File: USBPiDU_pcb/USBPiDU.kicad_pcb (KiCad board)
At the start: 2 copper layers, 71.5 x 56 mm, 39 parts, among them J1 USB_OTG, J2 ICSP, J3 Load Rail Input, P1 USB_A, P2 USB_A, P3 USB_A, P4 USB_A, P5 USB_A, P6 USB_A, U1 FT232RL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

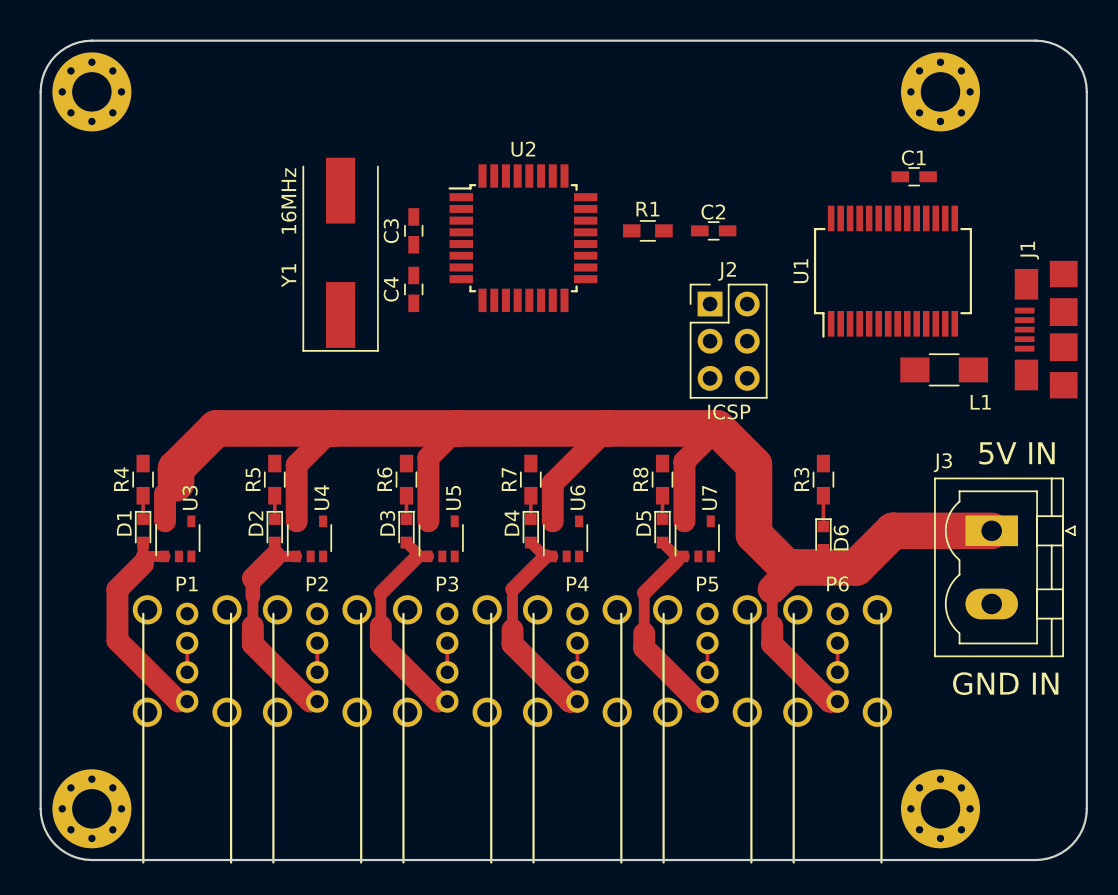
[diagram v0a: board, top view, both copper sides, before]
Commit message: Final v0.1 board layout
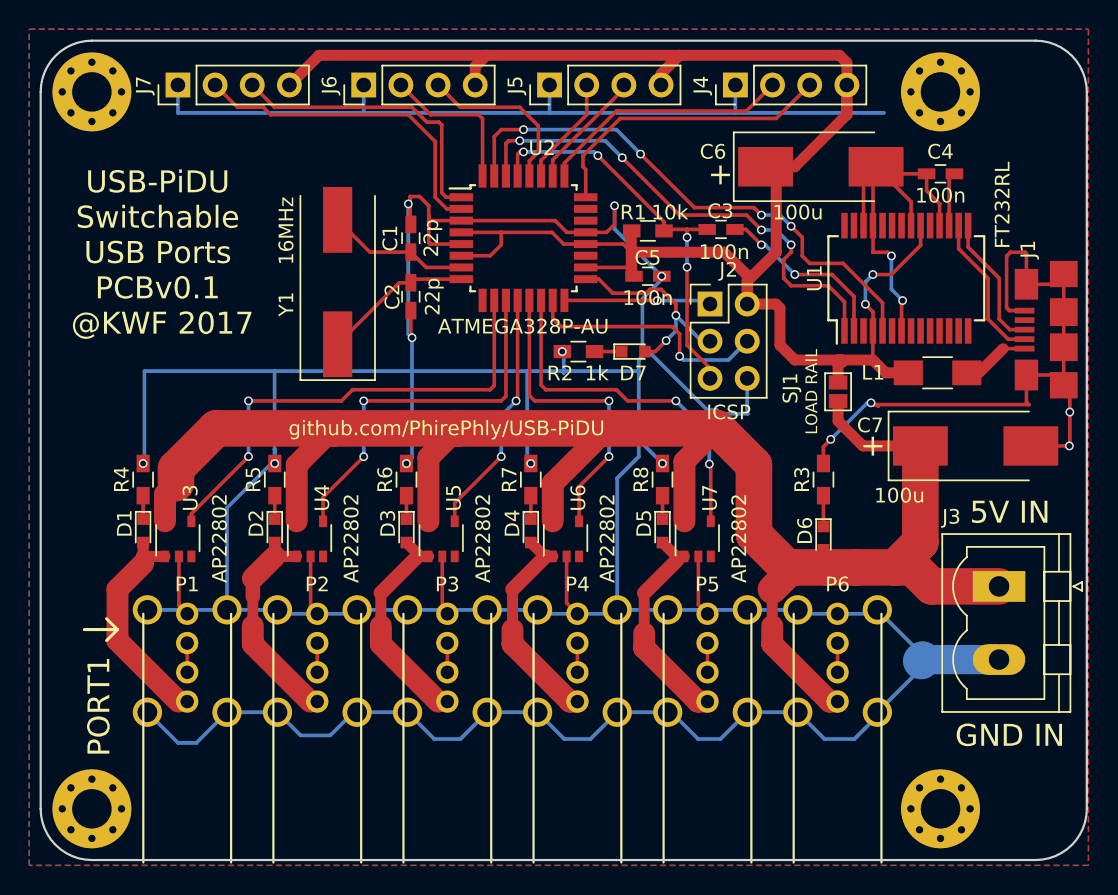
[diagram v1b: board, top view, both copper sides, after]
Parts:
- added C5: 100n, Capacitors_SMD:C_0603_HandSoldering, F.Cu at (88.0, 62.6)
- added C6: 100u, Capacitors_Tantalum_SMD:CP_Tantalum_Case-X_EIA-7343-43_Hand, F.Cu at (99.8, 55.1)
- added C7: 100u, Capacitors_Tantalum_SMD:CP_Tantalum_Case-X_EIA-7343-43_Hand, F.Cu at (110.4, 74.2)
- added D7: LED, LEDs:LED_0603, F.Cu at (87.0, 67.8)
- added J4: CONN_01X04, Pin_Headers:Pin_Header_Straight_1x04_Pitch2.54mm, F.Cu at (94.0, 49.5)
- added J5: CONN_01X04, Pin_Headers:Pin_Header_Straight_1x04_Pitch2.54mm, F.Cu at (81.3, 49.5)
- added J6: CONN_01X04, Pin_Headers:Pin_Header_Straight_1x04_Pitch2.54mm, F.Cu at (68.6, 49.5)
- added J7: CONN_01X04, Pin_Headers:Pin_Header_Straight_1x04_Pitch2.54mm, F.Cu at (55.9, 49.5)
- added R2: 1k, Resistors_SMD:R_0603_HandSoldering, F.Cu at (83.2, 67.8)
- added SJ1: LOAD RAIL, Connectors:GS2, F.Cu at (101.0, 70.5)
- C1, C2: value 100n -> 22p
- C3, C4: value 22p -> 100n
- J1: value USB_OTG -> 609-4613-1-ND
- moved C4 36.9 mm to (108.0, 55.6), turned to 0 degrees
- moved C1 34.7 mm to (71.8, 60.0), turned to 270 degrees
- moved C2 21.2 mm to (71.8, 64.0), turned to 90 degrees
- moved C3 21.0 mm to (93.0, 59.4), turned to 0 degrees
- moved J3 3.83 mm to (112.0, 83.8)
- moved Y1 2.01 mm to (66.8, 63.0)
- moved U1 1.04 mm to (105.7, 62.7)
- moved L1 0.49 mm to (107.8, 69.2)
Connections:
- C2 pad 1: RESET -> GND
- C3 pad 1: GND -> RESET
- MK1 pad 1: GND -> (no net)
- MK2 pad 1: GND -> (no net)
- MK3 pad 1: GND -> (no net)
- MK4 pad 1: GND -> (no net)
- U1 pad 17: Net-(C1-Pad2) -> Net-(C4-Pad2)
- U1 pad 2: Net-(C2-Pad2) -> Net-(C3-Pad2)
- U2 pad 1: P2_CTL -> DIO3
- U2 pad 10: P5_CTL -> P1_CTL
- U2 pad 11: (no net) -> P2_CTL
- U2 pad 12: (no net) -> P3_CTL
- U2 pad 13: (no net) -> P4_CTL
- U2 pad 14: (no net) -> P5_CTL
- U2 pad 2: P3_CTL -> DIO4
- U2 pad 24: (no net) -> AI1
- U2 pad 25: (no net) -> AI2
- U2 pad 26: (no net) -> AI3
- U2 pad 27: (no net) -> AI4
- U2 pad 28: (no net) -> AI5
- U2 pad 32: P1_CTL -> DIO2
- U2 pad 7: Net-(C3-Pad2) -> Net-(C1-Pad2)
- U2 pad 8: Net-(C4-Pad2) -> Net-(C2-Pad2)
- U2 pad 9: P4_CTL -> (no net)
- Y1 pad 1: Net-(C4-Pad2) -> Net-(C2-Pad2)
- Y1 pad 2: Net-(C3-Pad2) -> Net-(C1-Pad2)
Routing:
- net GND: track 0.00 -> 437.5 mm, vias 0 -> 16
- net +5V: track 0.00 -> 128.3 mm, vias 0 -> 2
- net TXD: track 0.00 -> 37.0 mm, vias 0 -> 4
- net RXD: track 0.00 -> 34.0 mm, vias 0 -> 4
- net P1_CTL: track 0.00 -> 32.9 mm, vias 0 -> 2
- net RESET: track 0.00 -> 28.1 mm, vias 0 -> 4
- net P2_CTL: track 0.00 -> 25.8 mm, vias 0 -> 2
- net P5_CTL: track 0.00 -> 24.7 mm, vias 0 -> 2
- net DIO4: track 0.00 -> 22.6 mm
- net P4_CTL: track 0.00 -> 21.2 mm, vias 0 -> 2
- net AI1: track 0.00 -> 20.4 mm
- net DIO3: track 0.00 -> 20.2 mm
- net AI2: track 0.00 -> 17.3 mm
- net Net-(J2-Pad4): track 0.00 -> 17.1 mm, vias 0 -> 1
- net P3_CTL: track 0.00 -> 16.9 mm, vias 0 -> 2
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- added copper zone on B.Cu, net GND
- added copper zone on F.Cu, net GND
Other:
- board text added: "+"
- board text added: "+5V"
- board text added: "AI1"
- board text added: "AI2"
- board text added: "AI3"
- board text added: "AI4"
- board text added: "AI5"
- board text added: "ALWAYS ON"
- board text added: "DIO2"
- board text added: "DIO3"
- board text added: "DIO4"
- board text added: "GND"
- board text added: "KennethFinnegan2007@Gmail.com blog.thelifeofkenneth.com Serial Port: 9600baud Turn on port N: +N Turn off port N: -N"
- board text added: "PORT 1"
- board text added: "PORT 2"
- board text added: "PORT 3"
- board text added: "PORT 4"
- board text added: "PORT 5"
- board text added: "PORT1"
- board text added: "Spare IO -->"
- board text added: "USB-PiDU Switchable USB Ports PCBv0.1 @KWF 2017"
- board text added: "d('-')"
- board text added: "github.com/PhirePhly/USB-PiDU"

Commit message: Changed pad clearance to 0.075mm (3thou)
The KiCAD global clearance default of 0.2mm is comically large,
and wipes out things like LED polarity silk, all mask between pads on
ICs, etc.

Closed #2
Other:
- rule pad_to_mask_clearance: 0.2 -> 0.075
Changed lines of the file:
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@@
     (links 146)
     (no_connects 0)
-    (area 46.424999 46.424999 118.075001 102.575001)
+    (area 42.585714 44.745 119.025001 104.325001)
     (thickness 1.6)
     (drawings 45)
@@
     (pad_size 1.524 1.524)
     (pad_drill 0.762)
-    (pad_to_mask_clearance 0.2)
+    (pad_to_mask_clearance 0.075)
     (aux_axis_origin 0 0)
     (visible_elements FFFFFF7F)
@@
   (gr_arc (start 50 99) (end 50 102.5) (angle 90) (layer Edge.Cuts) (width 0.15))
   (gr_line (start 46.5 50) (end 46.5 99) (angle 90) (layer Edge.Cuts) (width 0.15))
-  (via (at 82.15 67.75) (size 0.6) (drill 0.4) (layers F.Cu B.Cu) (net 1) (status C00000))
+  (via (at 82.15 67.75) (size 0.6) (drill 0.4) (layers F.Cu B.Cu) (net 1))
   (segment (start 82.25 69.25) (end 82.25 67.85) (width 0.25) (layer B.Cu) (net 1))
-  (segment (start 82.25 67.85) (end 82.15 67.75) (width 0.25) (layer B.Cu) (net 1) (status 800000))
+  (segment (start 82.25 67.85) (end 82.15 67.75) (width 0.25) (layer B.Cu) (net 1))
   (segment (start 100 74.5) (end 100 74.25) (width 0.25) (layer F.Cu) (net 1))
   (segment (start 103.624 71.374) (end 103.75 71.5) (width 0.25) (layer F.Cu) (net 1))
@@
   (segment (start 73.914 56.896) (end 73.914 52.266002) (width 0.25) (layer F.Cu) (net 45))
   (segment (start 74.218 57.2) (end 73.914 56.896) (width 0.25) (layer F.Cu) (net 45))
-  (segment (start 87.8 67.75) (end 88.5 67.75) (width 0.25) (layer F.Cu) (net 46) (status 400000))
+  (segment (start 87.8 67.75) (end 88.5 67.75) (width 0.25) (layer F.Cu) (net 46))
   (segment (start 89.916 66.334) (end 89.916 65.278) (width 0.25) (layer B.Cu) (net 46))
   (segment (start 89.25 67) (end 89.916 66.334) (width 0.25) (layer B.Cu) (net 46))
@@
   (segment (start 87.884 63.754) (end 88.138 63.5) (width 0.25) (layer F.Cu) (net 46))
   (segment (start 91.678 67.04) (end 92.25 67.04) (width 0.25) (layer B.Cu) (net 46))
-  (segment (start 84.35 67.75) (end 86.2 67.75) (width 0.25) (layer F.Cu) (net 47) (status C00000))
+  (segment (start 84.35 67.75) (end 86.2 67.75) (width 0.25) (layer F.Cu) (net 47))
   (zone (net 1) (net_name GND) (layer B.Cu) (hatch edge 0.508)
     (connect_pads (clearance 0.508))

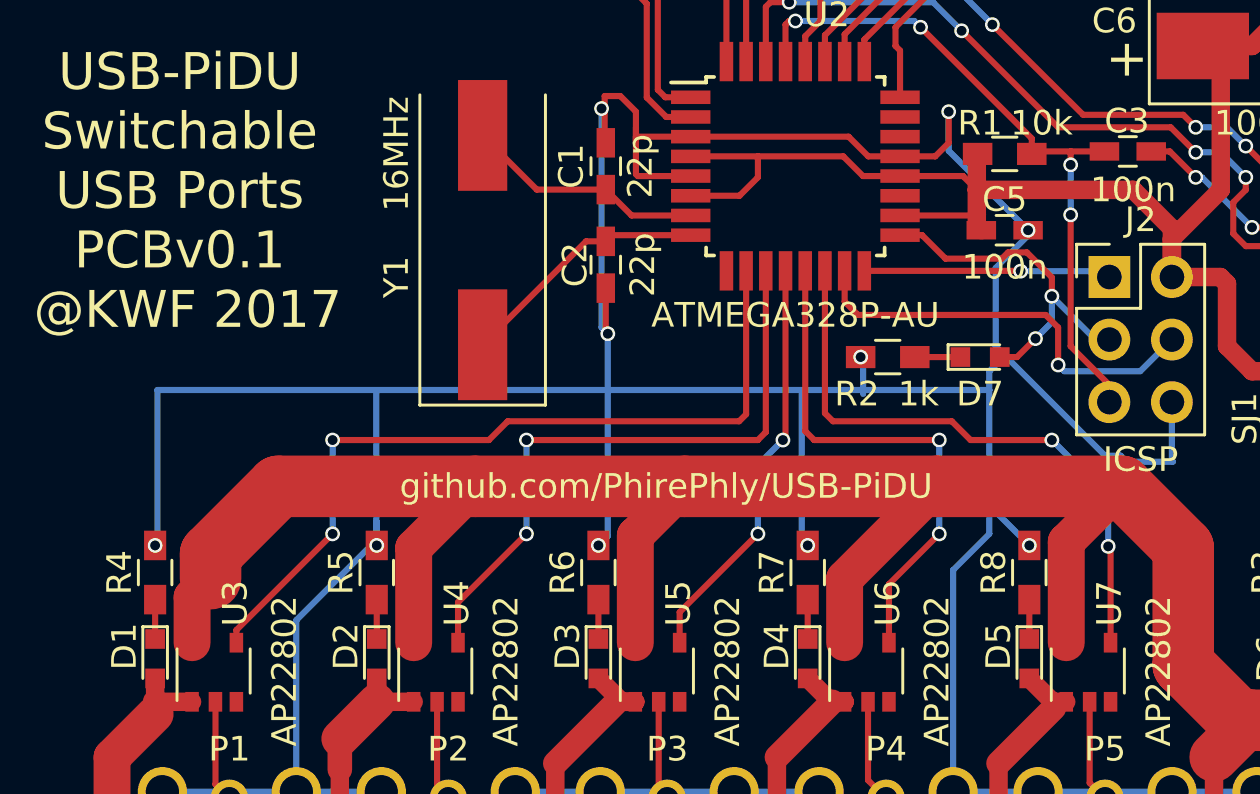
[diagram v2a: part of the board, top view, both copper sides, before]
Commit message: Moved vias off 0603 footprints
No need to place vias on footprints on final routing.

Closed #1
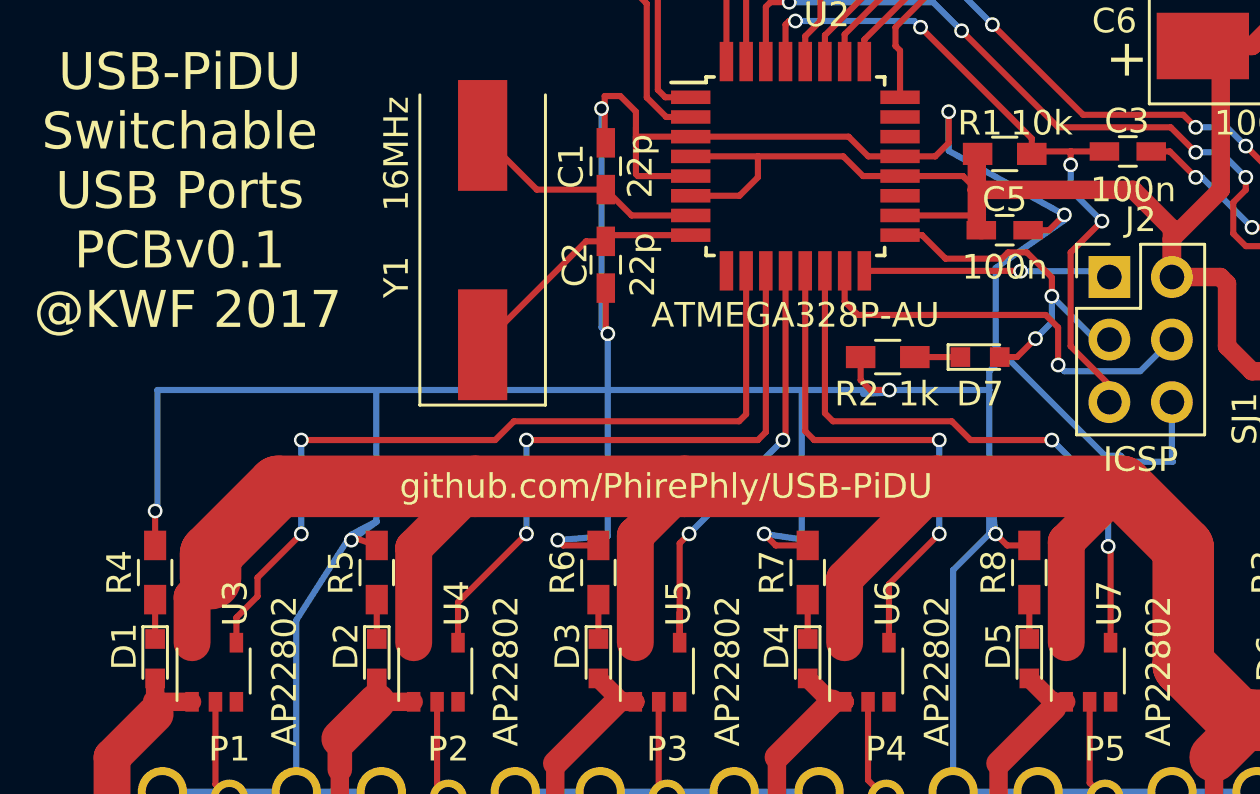
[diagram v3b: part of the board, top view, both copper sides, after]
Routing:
- net GND: track 437.5 -> 452.0 mm
- net P3_CTL: track 16.9 -> 18.1 mm
- net RESET: track 28.1 -> 29.1 mm
- net P1_CTL: track 32.9 -> 33.6 mm
